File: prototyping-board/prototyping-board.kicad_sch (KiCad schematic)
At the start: 44 parts, among them J1 Conn_01x02, J10 Conn_01x02, J11 Conn_01x03, J12 Conn_01x03, J13 Conn_01x03, J14 Conn_01x03, J15 Conn_01x03, J16 Conn_01x03, J17 Conn_01x03, J18 Conn_01x03, J19 Conn_01x03, J2 Conn_01x02, J20 Conn_01x03, J21 Conn_01x03, J22 Conn_01x03, J23 Conn_01x06, J24 Conn_01x06, J25 Conn_01x04, J26 Conn_01x04, J27 Conn_01x05, J28 Conn_01x05, J29 Conn_01x05, J3 Conn_01x02, J30 Conn_01x04, J31 Conn_01x04, J32 Conn_01x04, J33 Conn_01x03, J34 Conn_01x03, J35 Conn_01x03, J36 Conn_01x02, J37 Conn_01x02, J38 Conn_01x02, J4 Conn_01x02, J5 Conn_01x02, J6 Conn_01x02, J7 Conn_01x02, J8 Conn_01x02, J9 Conn_01x02, U1 MEGA_PRO_EMBED_CH340G___ATMEG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

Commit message: label improvements (#23)
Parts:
- H1, H2, H3, H4, U1: now left out of the parts list
- J1, J10, J2, J3, J36, J37, J38, J4, J5, J6, J7, J8, J9: LCSC (none) -> C158012
- J11, J12, J13, J14, J15, J16, J17, J18, J19, J20, J21, J22, J33, J34, J35: LCSC (none) -> C144394
- J23, J24: LCSC (none) -> C144397
- J25, J26, J30, J31, J32: LCSC (none) -> C144395
- J27, J28, J29: LCSC (none) -> C157991
- JP1: LCSC (none) -> C49257
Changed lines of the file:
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@@
+      (effects (font (size 1.27 1.27)) hide)
+    )
+    (property "LCSC" "C158012" (id 4) (at 217.932 103.632 0)
       (effects (font (size 1.27 1.27)) hide)
     )
@@
       (effects (font (size 1.27 1.27)) hide)
     )
+    (property "LCSC" "C158012" (id 4) (at 217.932 97.282 0)
+      (effects (font (size 1.27 1.27)) hide)
+    )
     (pin "1")
     (pin "2")
@@
       (effects (font (size 1.27 1.27)) hide)
     )
+    (property "LCSC" "C158012" (id 4) (at 217.932 90.932 0)
+      (effects (font (size 1.27 1.27)) hide)
+    )
     (pin "1")
     (pin "2")
@@
       (effects (font (size 1.27 1.27)) hide)
     )
+    (property "LCSC" "C158012" (id 4) (at 217.932 84.582 0)
+      (effects (font (size 1.27 1.27)) hide)
+    )
     (pin "1")
     (pin "2")
@@
       (effects (font (size 1.27 1.27)) hide)
     )
+    (property "LCSC" "C158012" (id 4) (at 217.932 78.232 0)
+      (effects (font (size 1.27 1.27)) hide)
+    )
     (pin "1")
     (pin "2")
@@
       (effects (font (size 1.27 1.27)) hide)
     )
+    (property "LCSC" "C158012" (id 4) (at 188.214 77.724 0)
+      (effects (font (size 1.27 1.27)) hide)
+    )
     (pin "1")
     (pin "2")
@@
       (effects (font (size 1.27 1.27)) hide)
     )
+    (property "LCSC" "C158012" (id 4) (at 188.214 84.074 0)
+      (effects (font (size 1.27 1.27)) hide)
+    )
     (pin "1")
     (pin "2")
@@
       (effects (font (size 1.27 1.27)) hide)
     )
+    (property "LCSC" "C158012" (id 4) (at 188.214 90.424 0)
+      (effects (font (size 1.27 1.27)) hide)
+    )
     (pin "1")
     (pin "2")
@@
       (effects (font (size 1.27 1.27)) hide)
     )
+    (property "LCSC" "C158012" (id 4) (at 188.214 96.774 0)
+      (effects (font (size 1.27 1.27)) hide)
+    )
     (pin "1")
     (pin "2")
@@
       (effects (font (size 1.27 1.27)) hide)
     )
+    (property "LCSC" "C158012" (id 4) (at 188.214 103.124 0)
+      (effects (font (size 1.27 1.27)) hide)
+    )
     (pin "1")
     (pin "2")
@@
       (effects (font (size 1.27 1.27)) hide)
     )
+    (property "LCSC" "C144394" (id 4) (at 118.618 75.438 0)
+      (effects (font (size 1.27 1.27)) hide)
+    )
     (pin "1")
     (pin "2")
@@
       (effects (font (size 1.27 1.27)) hide)
     )
+    (property "LCSC" "C144394" (id 4) (at 118.618 84.328 0)
+      (effects (font (size 1.27 1.27)) hide)
+    )
     (pin "1")
     (pin "2")
@@
       (effects (font (size 1.27 1.27)) hide)
     )
+    (property "LCSC" "C144394" (id 4) (at 118.618 93.218 0)
+      (effects (font (size 1.27 1.27)) hide)
+    )
     (pin "1")
     (pin "2")
@@
       (effects (font (size 1.27 1.27)) hide)
     )
+    (property "LCSC" "C144394" (id 4) (at 118.618 102.108 0)
+      (effects (font (size 1.27 1.27)) hide)
+    )
     (pin "1")
     (pin "2")
@@
       (effects (font (size 1.27 1.27)) hide)
     )
+    (property "LCSC" "C144394" (id 4) (at 118.618 110.998 0)
+      (effects (font (size 1.27 1.27)) hide)
+    )
     (pin "1")
     (pin "2")
@@
       (effects (font (size 1.27 1.27)) hide)
     )
+    (property "LCSC" "C144394" (id 4) (at 154.178 75.692 0)
+      (effects (font (size 1.27 1.27)) hide)
+    )
     (pin "1")
     (pin "2")
@@
       (effects (font (size 1.27 1.27)) hide)
     )
+    (property "LCSC" "C144394" (id 4) (at 154.178 84.582 0)
+      (effects (font (size 1.27 1.27)) hide)
+    )
     (pin "1")
     (pin "2")
@@
       (effects (font (size 1.27 1.27)) hide)
     )
+    (property "LCSC" "C144394" (id 4) (at 154.178 93.472 0)
+      (effects (font (size 1.27 1.27)) hide)
+    )
     (pin "1")
     (pin "2")
@@
       (effects (font (size 1.27 1.27)) hide)
     )
+    (property "LCSC" "C144394" (id 4) (at 154.178 102.362 0)
+      (effects (font (size 1.27 1.27)) hide)
+    )
     (pin "1")
     (pin "2")
@@
       (effects (font (size 1.27 1.27)) hide)
     )
+    (property "LCSC" "C144394" (id 4) (at 154.178 111.252 0)
+      (effects (font (size 1.27 1.27)) hide)
+    )
     (pin "1")
     (pin "2")
@@
       (effects (font (size 1.27 1.27)) hide)
     )
+    (property "LCSC" "C144394" (id 4) (at 105.918 154.94 0)
+      (effects (font (size 1.27 1.27)) hide)
+    )
     (pin "1")
     (pin "2")
@@
       (effects (font (size 1.27 1.27)) hide)
     )
+    (property "LCSC" "C144394" (id 4) (at 105.918 146.05 0)
+      (effects (font (size 1.27 1.27)) hide)
+    )
     (pin "1")
     (pin "2")
@@
       (effects (font (size 1.27 1.27)) hide)
     )
+    (property "LCSC" "C144395" (id 4) (at 146.05 19.304 0)
+      (effects (font (size 1.27 1.27)) hide)
+    )
     (pin "1")
     (pin "2")
@@
       (effects (font (size 1.27 1.27)) hide)
     )
+    (property "LCSC" "C144395" (id 4) (at 161.036 19.812 0)
+      (effects (font (size 1.27 1.27)) hide)
+    )
     (pin "1")
     (pin "2")
@@
     )
     (property "Datasheet" "~" (id 3) (at 177.038 153.924 0)
+      (effects (font (size 1.27 1.27)) hide)
+    )
+    (property "LCSC" "C157991" (id 4) (at 177.038 153.924 0)
       (effects (font (size 1.27 1.27)) hide)
     )
@@
       (effects (font (size 1.27 1.27)) hide)
     )
+    (property "LCSC" "C157991" (id 4) (at 163.068 153.924 0)
+      (effects (font (size 1.27 1.27)) hide)
+    )
     (pin "1")
     (pin "2")
@@
       (effects (font (size 1.27 1.27)) hide)
     )
+    (property "LCSC" "C144394" (id 4) (at 240.03 149.86 0)
+      (effects (font (size 1.27 1.27)) hide)
+    )
     (pin "1")
     (pin "2")
@@
       (effects (font (size 1.27 1.27)) hide)
     )
+    (property "LCSC" "C144394" (id 4) (at 231.14 149.86 0)
+      (effects (font (size 1.27 1.27)) hide)
+    )
     (pin "1")
     (pin "2")
@@
       (effects (font (size 1.27 1.27)) hide)
     )
+    (property "LCSC" "C144394" (id 4) (at 222.25 149.86 0)
+      (effects (font (size 1.27 1.27)) hide)
+    )
     (pin "1")
     (pin "2")
@@
       (effects (font (size 1.27 1.27)) hide)
     )
+    (property "LCSC" "C144395" (id 4) (at 256.286 78.232 0)
+      (effects (font (size 1.27 1.27)) hide)
+    )
     (pin "1")
     (pin "2")
@@
       (effects (font (size 1.27 1.27)) hide)
     )
+    (property "LCSC" "C144395" (id 4) (at 256.286 89.662 0)
+      (effects (font (size 1.27 1.27)) hide)
+    )
     (pin "1")
     (pin "2")
@@
       (effects (font (size 1.27 1.27)) hide)
     )
+    (property "LCSC" "C144395" (id 4) (at 256.286 101.092 0)
+      (effects (font (size 1.27 1.27)) hide)
+    )
     (pin "1")
     (pin "2")
@@
     )
     (property "Datasheet" "~" (id 3) (at 208.28 17.78 0)
+      (effects (font (size 1.27 1.27)) hide)
+    )
+    (property "LCSC" "C157991" (id 4) (at 208.28 17.78 0)
       (effects (font (size 1.27 1.27)) hide)
     )
@@
     )
     (property "Datasheet" "~" (id 3) (at 87.122 22.352 0)
+      (effects (font (size 1.27 1.27)) hide)
+    )
+    (property "LCSC" "C144397" (id 4) (at 87.122 22.352 0)
       (effects (font (size 1.27 1.27)) hide)
     )
@@
       (effects (font (size 1.27 1.27)) hide)
     )
+    (property "LCSC" "C144397" (id 4) (at 103.632 22.352 0)
+      (effects (font (size 1.27 1.27)) hide)
+    )
     (pin "1")
     (pin "2")
@@
   )
   (symbol (lib_id "MEGA_PRO_EMBED_CH340G___ATMEGA2560:MEGA_PRO_EMBED_CH340G___ATMEGA2560") (at 50.292 101.6 0) (unit 1)
-    (in_bom yes) (on_board yes)
+    (in_bom no) (on_board yes)
     (property "Reference" "U1" (id 0) (at 125.476 96.6216 90)
       (effects (font (size 1.27 1.27)) (justify right))
@@
       (effects (font (size 1.27 1.27)) hide)
     )
+    (property "LCSC" "C158012" (id 4) (at 240.03 31.242 0)
+      (effects (font (size 1.27 1.27)) hide)
+    )
     (pin "1")
     (pin "2")
@@
       (effects (font (size 1.27 1.27)) hide)
     )
+    (property "LCSC" "C49257" (id 4) (at 263.652 28.702 0)
+      (effects (font (size 1.27 1.27)) hide)
+    )
     (pin "1")
     (pin "2")
@@
   )
   (symbol (lib_id "Mechanical:MountingHole") (at 60.706 189.23 0) (unit 1)
-    (in_bom yes) (on_board yes) (fields_autoplaced)
+    (in_bom no) (on_board yes) (fields_autoplaced)
     (property "Reference" "H4" (id 0) (at 64.008 187.9599 0)
       (effects (font (size 1.27 1.27)) (justify left))
@@
       (effects (font (size 1.27 1.27)) hide)
     )
+    (property "LCSC" "C158012" (id 4) (at 188.214 109.982 0)
+      (effects (font (size 1.27 1.27)) hide)
+    )
     (pin "1")
     (pin "2")
   )
   (symbol (lib_id "Mechanical:MountingHole") (at 37.846 181.864 0) (unit 1)
-    (in_bom yes) (on_board yes) (fields_autoplaced)
+    (in_bom no) (on_board yes) (fields_autoplaced)
     (property "Reference" "H1" (id 0) (at 40.64 180.5939 0)
       (effects (font (size 1.27 1.27)) (justify left))
@@
   )
   (symbol (lib_id "mobiflight:LOGO") (at 113.284 183.896 0) (unit 1)
-    (in_bom yes) (on_board yes) (fields_autoplaced)
+    (in_bom no) (on_board yes) (fields_autoplaced)
     (property "Reference" "#G1" (id 0) (at 113.284 175.0936 0)
       (effects (font (size 1.27 1.27)) hide)
@@
   )
   (symbol (lib_id "Mechanical:MountingHole") (at 60.96 181.864 0) (unit 1)
-    (in_bom yes) (on_board yes)
+    (in_bom no) (on_board yes)
     (property "Reference" "H2" (id 0) (at 64.262 180.5939 0)
       (effects (font (size 1.27 1.27)) (justify left))
@@
   )
   (symbol (lib_id "Mechanical:MountingHole") (at 37.846 189.23 0) (unit 1)
-    (in_bom yes) (on_board yes) (fields_autoplaced)
+    (in_bom no) (on_board yes) (fields_autoplaced)
     (property "Reference" "H3" (id 0) (at 41.148 187.9599 0)
       (effects (font (size 1.27 1.27)) (justify left))
@@
       (effects (font (size 1.27 1.27)) hide)
     )
+    (property "LCSC" "C158012" (id 4) (at 217.932 109.982 0)
+      (effects (font (size 1.27 1.27)) hide)
+    )

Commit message: Use boomelect XH connectors
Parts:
- J1, J10, J2, J3, J36, J37, J38, J4, J5, J6, J7, J8, J9: LCSC C158012 -> C20079
- J11, J12, J13, J14, J15, J16, J17, J18, J19, J20, J21, J22, J33, J34, J35: LCSC C144394 -> C2316
- J23, J24: LCSC C144397 -> C5663
- J25, J26, J30, J31, J32: LCSC C144395 -> C37815
- J27, J28, J29: LCSC C157991 -> C2318

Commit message: Update all boards to KiCad 9.0 (#44)
* update dimmer board to KiCad version 9

* update dual encoder board to KiCad version 9

* update input shifter board, start numbering with zero instead one

* update MAX7219 breakout board to KiCad version 9

* add 3 pol JST connector

* updatge template to KiCad version 9

* update potentiometer board to KiCad version 9, use JST connector from MF lib

* update 6pin JST connector

* update prototyping board to KiCad version 9

* update symbols on dimmer board, fixed DRC

* update symbols from MAX7219 breakout board

* add Screw Terminalblocks to footprint lib and 3D models

* use screw terminals from MF lib

* fixed outline of Potentiometer board

* fixed missing IDC footprints error

* add MAX7219 symbol

* use MAX7219 symbol from MF lib

* add Mega2560mini symbol and footprint to MF library

* use Mega2560mini symbol and footprint from MF library

* add used Dual Encoder symbol and footprint to MF lib

* use footprint and symbol for Dual Encoder from MF lib
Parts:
- U1: footprint MODULE_MEGA_PRO_EMBED_CH340G_:_ATMEGA2560 -> MobiFlight:Mega_2560_mini; symbol MEGA_PRO_EMBED_CH340G___ATMEGA2560:MEGA_PRO_EMBED_CH340G___ATMEGA2560 -> mobiflight-library:MEGA_PRO_EMBED_CH340G___ATMEGA2560; now in the parts list

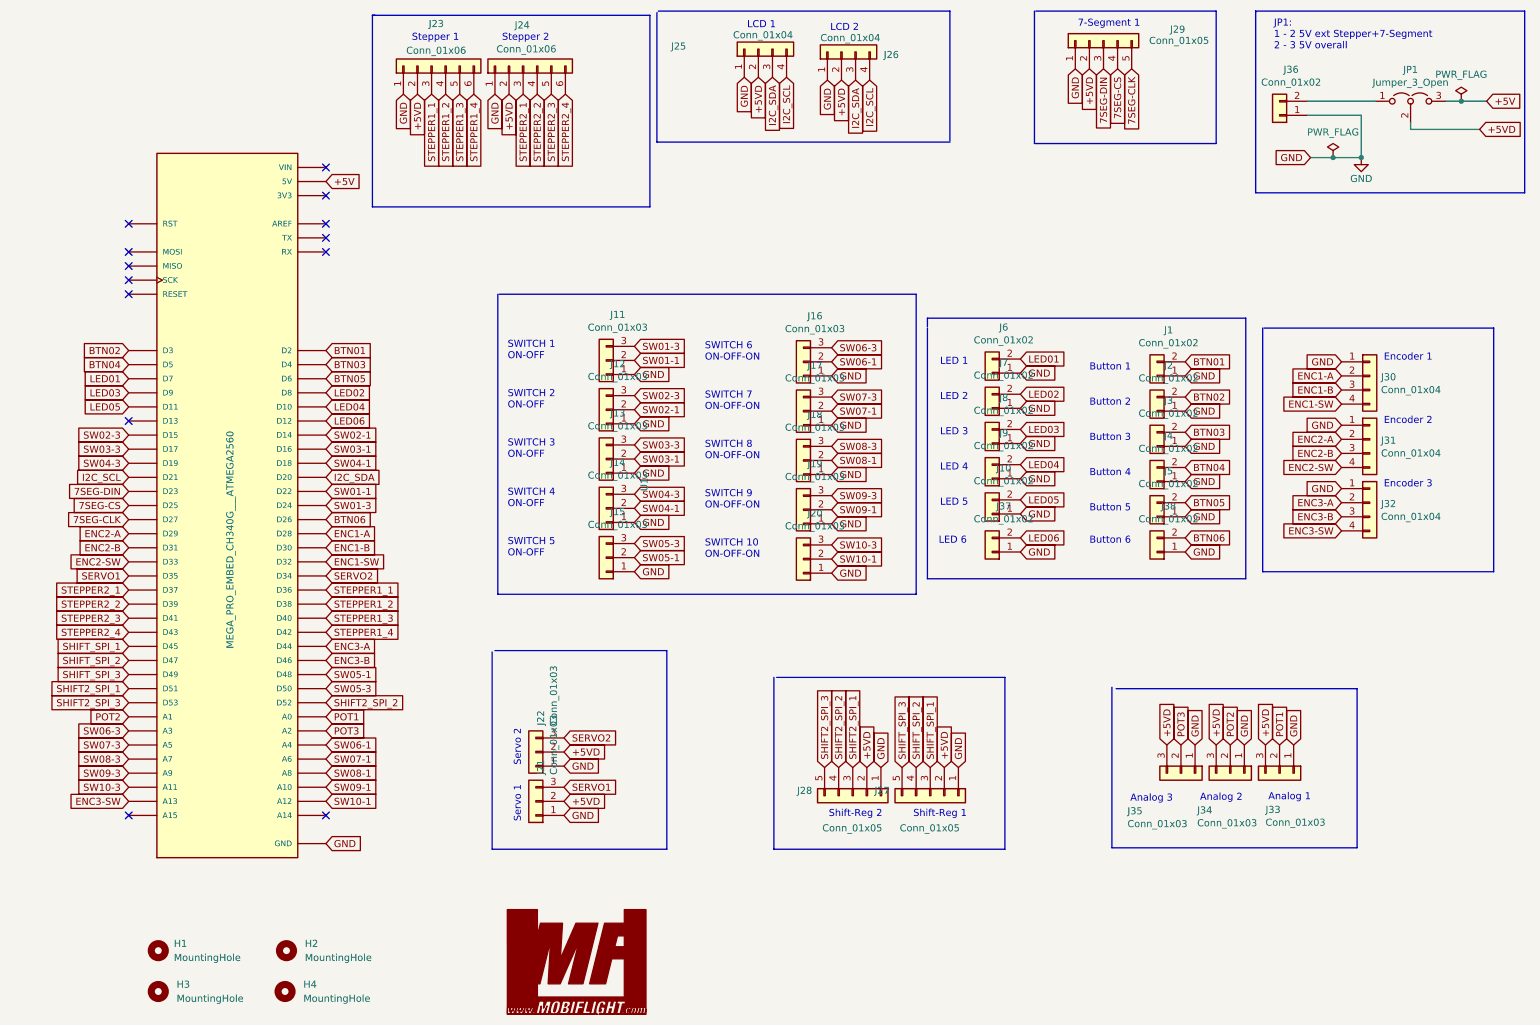
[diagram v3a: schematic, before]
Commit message: add diode, add 4th Encoder, new position of PWR
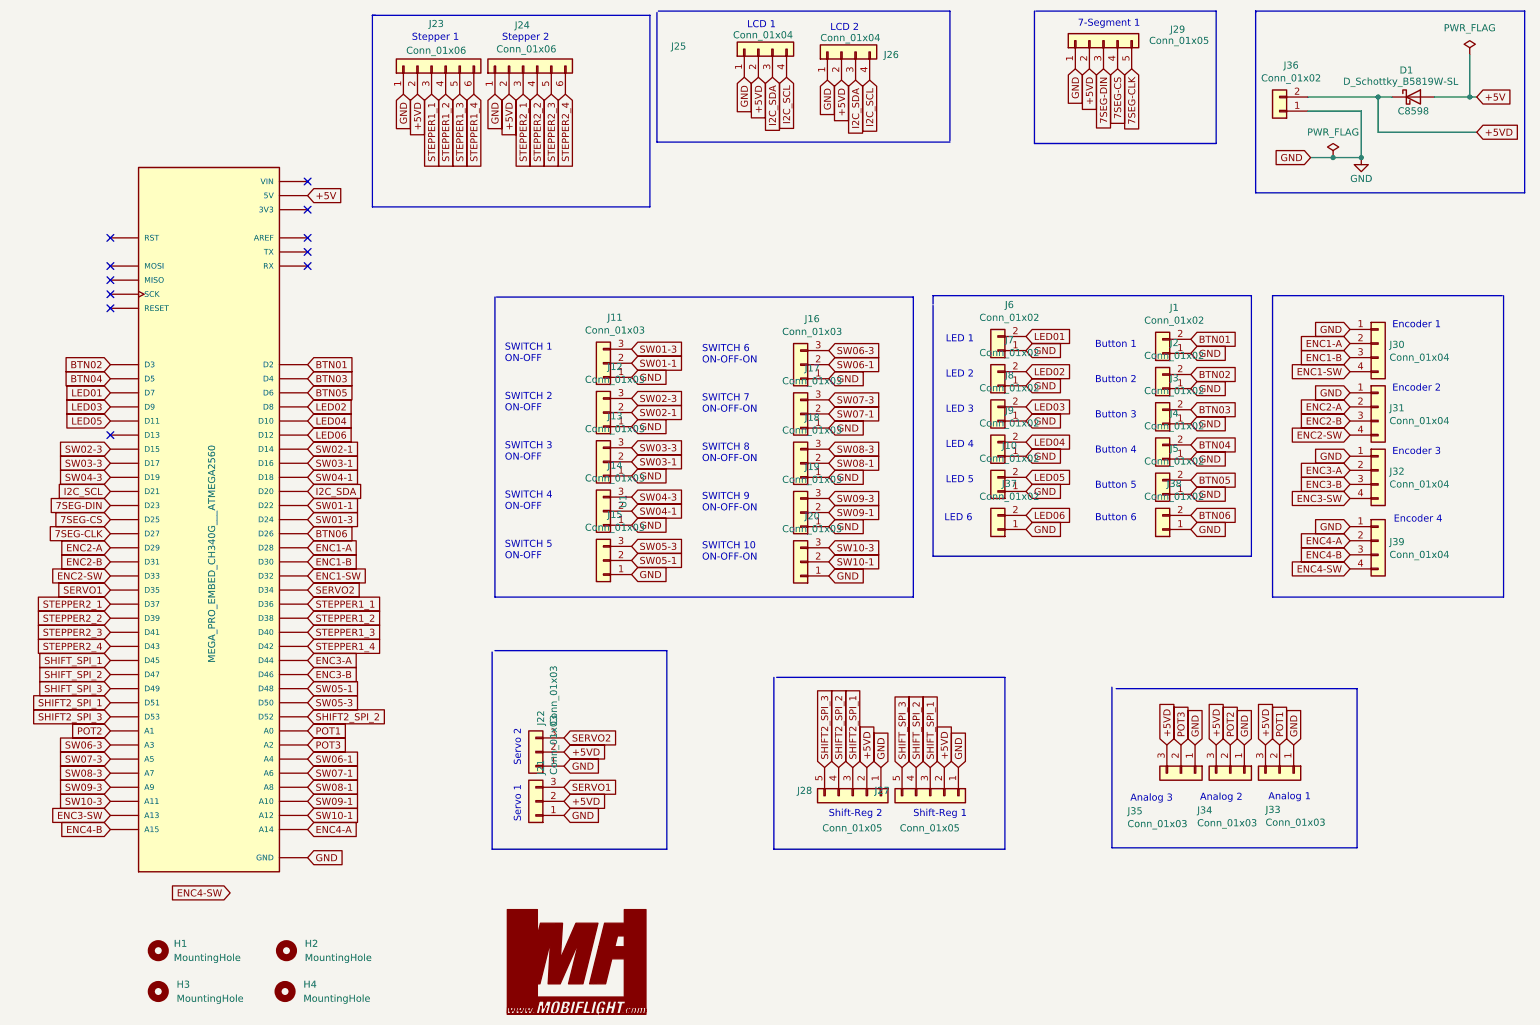
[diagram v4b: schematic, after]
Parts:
- removed JP1: Jumper_3_Open, Connector_PinHeader_2.54mm:PinHeader_1x03_P2.54mm_Vertical, symbol Jumper:Jumper_3_Open
- added D1: D_Schottky_B5819W-SL, Diode_SMD:D_SOD-123, symbol MobiFlight:D_Schottky_B5819W-SL
- added J39: Conn_01x04, Connector_JST:JST_XH_B4B-XH-A_1x04_P2.50mm_Vertical, symbol Connector_Generic:Conn_01x04
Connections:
- net +5V: now also D1.2 (A)
- net +5VD: now also J36.2 (Pin_2), D1.1 (K)
- net GND: now also J39.1 (Pin_1)
- net ENC4-A: now reaches U1.A14
- net ENC4-A: now also J39.2 (Pin_2)
- net ENC4-B: now reaches U1.A15
- net ENC4-B: now also J39.3 (Pin_3)
- new net ENC4-SW: J39.4 (Pin_4)
- no-connect marks 13 -> 11
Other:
- note added: "Encoder 4"
- note removed: "JP1: 1 - 2 5V ext Stepper+7-Segment 2 - 3 5V overall"
- moved on the sheet: J1, J10, J11, J12, J13, J14, J15, J16, J17, J18, J19, J2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

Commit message: PWR connector in red, some optimazations
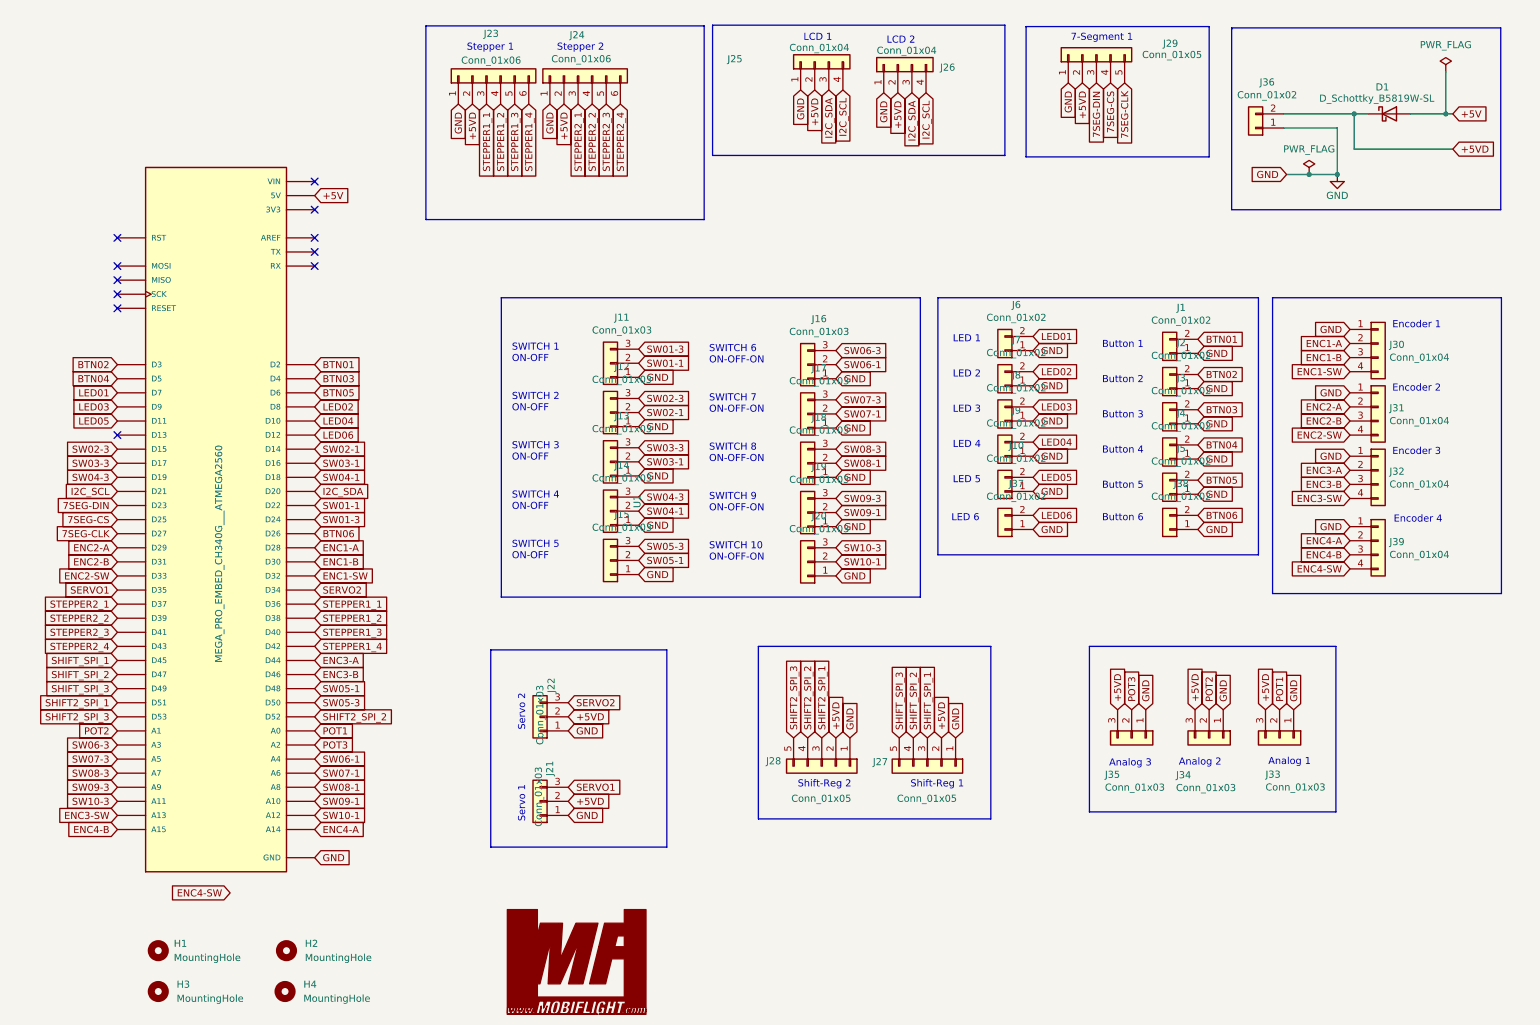
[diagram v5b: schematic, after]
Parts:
- J36: LCSC C20079 -> C24192
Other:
- moved on the sheet: D1, J1, J10, J11, J12, J13, J14, J15, J16, J17, J18, J19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
